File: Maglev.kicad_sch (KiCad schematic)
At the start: 25 parts, among them J1 629722000214, J2 691103110002, J3 61300621121, J4 61300821121, U1 WE-TVS-82400102, U2 ESP32-C3

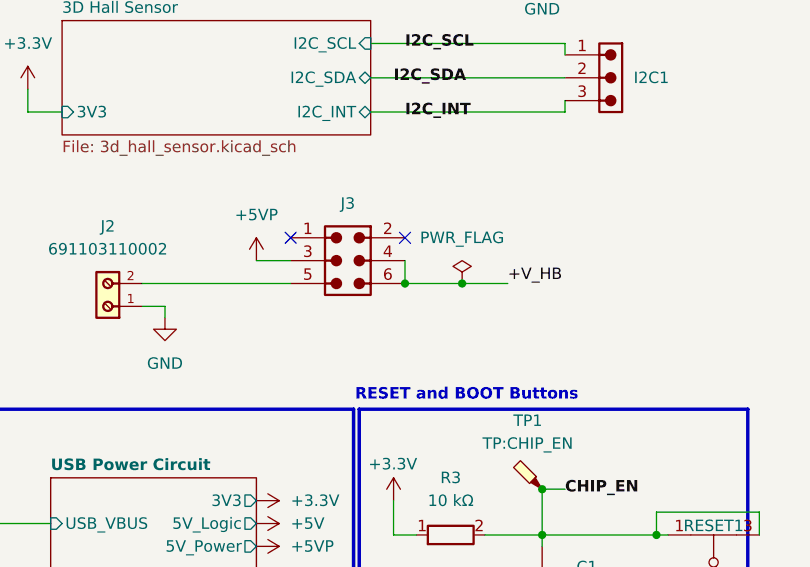
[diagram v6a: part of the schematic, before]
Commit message: Edit symbol libraries for BOM
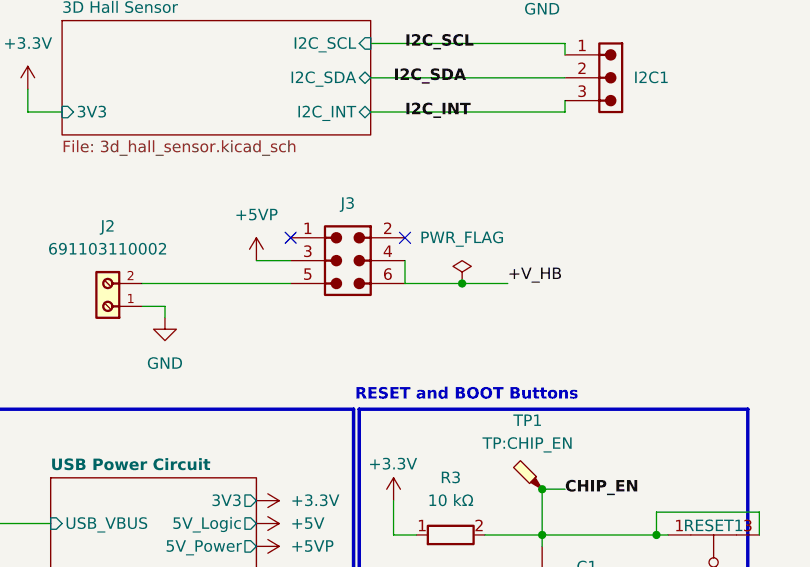
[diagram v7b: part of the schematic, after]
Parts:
- I2C1: symbol Connector_Wurth_WR-PHD:61300311121 -> Connector_Wurth_WR-PHD_CUSTOM:61300311121; Part Number (none) -> 61300311121
- J1: MF Würth Elektronik -> (none); MP 629722000214 -> (none); Manufacturer (none) -> Würth Elektronik; Part Number (none) -> 629722000214
- J2: MF Wurth Electronics -> (none); MP 691103110002 -> (none); Manufacturer (none) -> Wurth Electronics; Part Number (none) -> 691103110002
- J3: symbol Connector_Wurth_WR-PHD:61300621121 -> Connector_Wurth_WR-PHD_CUSTOM:61300621121; Part Number (none) -> 61300621121
- J4: symbol Connector_Wurth_WR-PHD:61300821121 -> Connector_Wurth_WR-PHD_CUSTOM:61300821121; Part Number (none) -> 61300821121
- U1: symbol Power_Protection:WE-TVS-82400102 -> Power_Protection_CUSTOM:WE-TVS-82400102; Manufacturer (none) -> Wurth Elektronik; Part Number (none) -> 82400102
- U2: Manufacturer (none) -> Espressif; Part Number (none) -> ESP32-C3
- UART1: symbol Connector_Wurth_WR-PHD:61300211121 -> Connector_Wurth_WR-PHD_CUSTOM:61300211121; Part Number (none) -> 61300211121
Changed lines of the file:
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@@
 		(color 0 0 0 0)
 	)
-	(junction
-		(at 109.22 116.84)
-		(diameter 0)
-		(color 0 0 0 0)
-	)
 	(no_connect
 		(at 45.72 146.05)
@@
 	)
 	(symbol
-		(lib_id "Connector_Wurth_WR-PHD:61300821121")
+		(lib_id "Connector_Wurth_WR-PHD_CUSTOM:61300821121")
 		(at 140.97 25.4 90)
 		(unit 1)
@@
 			)
 		)
+		(property "Part Number" "61300821121"
+			(at 140.97 25.4 0)
+			(hide yes)
+			(show_name no)
+			(do_not_autoplace no)
+			(effects
+				(font
+					(size 1.27 1.27)
+				)
+			)
+		)
 		(pin "1"
 		)
@@
 			)
 		)
-		(property "Datasheet" ""
+		(property "Datasheet" "https://www.we-online.com/components/products/datasheet/629722000214.pdf?srsltid=AfmBOopgS1fpVqzIp88kkSziMYYixj-iXYRL22aRdxcRBDhgIMAZGuSl"
 			(at 30.48 148.59 0)
 			(hide yes)
@@
 			)
 		)
-		(property "MF" "Würth Elektronik"
+		(property "Package" "None"
 			(at 30.48 148.59 0)
 			(hide yes)
@@
 			)
 		)
-		(property "Package" "None"
+		(property "Price" "None"
 			(at 30.48 148.59 0)
 			(hide yes)
@@
 			)
 		)
-		(property "Price" "None"
+		(property "SnapEDA_Link" "https://www.snapeda.com/parts/629722000214/W%25C3%25BCrth+Elektronik+Midcom/view-part/?ref=snap"
 			(at 30.48 148.59 0)
 			(hide yes)
@@
 			)
 		)
-		(property "SnapEDA_Link" "https://www.snapeda.com/parts/629722000214/W%25C3%25BCrth+Elektronik+Midcom/view-part/?ref=snap"
+		(property "Availability" "In Stock"
 			(at 30.48 148.59 0)
 			(hide yes)
@@
 			)
 		)
-		(property "MP" "629722000214"
+		(property "Check_prices" "https://www.snapeda.com/parts/629722000214/W%25C3%25BCrth+Elektronik+Midcom/view-part/?ref=eda"
 			(at 30.48 148.59 0)
 			(hide yes)
@@
 			)
 		)
-		(property "Availability" "In Stock"
+		(property "Manufacturer" "Würth Elektronik"
 			(at 30.48 148.59 0)
 			(hide yes)
@@
 			)
 		)
-		(property "Check_prices" "https://www.snapeda.com/parts/629722000214/W%25C3%25BCrth+Elektronik+Midcom/view-part/?ref=eda"
+		(property "Part Number" "629722000214"
 			(at 30.48 148.59 0)
 			(hide yes)
@@
 			)
 		)
+		(property "Manufacturer" "Espressif"
+			(at 92.71 52.07 0)
+			(hide yes)
+			(show_name no)
+			(do_not_autoplace no)
+			(effects
+				(font
+					(size 1.27 1.27)
+				)
+			)
+		)
+		(property "Part Number" "ESP32-C3"
+			(at 92.71 52.07 0)
+			(hide yes)
+			(show_name no)
+			(do_not_autoplace no)
+			(effects
+				(font
+					(size 1.27 1.27)
+				)
+			)
+		)
 		(pin "1"
 		)
@@
 	)
 	(symbol
+		(lib_name "ElectromagneticActor_3")
 		(lib_id "Device:ElectromagneticActor")
 		(at 260.35 53.34 180)
@@
 	)
 	(symbol
-		(lib_name "TestPoint_Probe_1")
 		(lib_id "Connector:TestPoint_Probe")
 		(at 124.46 172.72 90)
@@
 	)
 	(symbol
+		(lib_name "ElectromagneticActor_2")
 		(lib_id "Device:ElectromagneticActor")
 		(at 260.35 40.64 180)
@@
 	)
 	(symbol
-		(lib_id "Power_Protection:WE-TVS-82400102")
+		(lib_id "Power_Protection_CUSTOM:WE-TVS-82400102")
 		(at 63.5 162.56 270)
 		(unit 1)
@@
 			)
 		)
+		(property "Manufacturer" "Wurth Elektronik"
+			(at 63.5 162.56 0)
+			(hide yes)
+			(show_name no)
+			(do_not_autoplace no)
+			(effects
+				(font
+					(size 1.27 1.27)
+				)
+			)
+		)
+		(property "Part Number" "82400102"
+			(at 63.5 162.56 0)
+			(hide yes)
+			(show_name no)
+			(do_not_autoplace no)
+			(effects
+				(font
+					(size 1.27 1.27)
+				)
+			)
+		)
 		(pin "6"
 		)
@@
 	)
 	(symbol
+		(lib_name "ElectromagneticActor_1")
 		(lib_id "Device:ElectromagneticActor")
 		(at 260.35 26.67 180)
@@
 	)
 	(symbol
-		(lib_id "Connector_Wurth_WR-PHD:61300621121")
+		(lib_id "Connector_Wurth_WR-PHD_CUSTOM:61300621121")
 		(at 102.87 114.3 270)
 		(unit 1)
@@
 			)
 		)
+		(property "Part Number" "61300621121"
+			(at 102.87 114.3 0)
+			(hide yes)
+			(show_name no)
+			(do_not_autoplace no)
+			(effects
+				(font
+					(size 1.27 1.27)
+				)
+			)
+		)
 		(pin "3"
 		)
@@
 	)
 	(symbol
-		(lib_id "Connector_Wurth_WR-PHD:61300211121")
+		(lib_id "Connector_Wurth_WR-PHD_CUSTOM:61300211121")
 		(at 172.72 24.13 270)
 		(unit 1)
@@
 			)
 		)
+		(property "Part Number" "61300211121"
+			(at 172.72 24.13 0)
+			(hide yes)
+			(show_name no)
+			(do_not_autoplace no)
+			(effects
+				(font
+					(size 1.27 1.27)
+				)
+			)
+		)
 		(pin "1"
 		)
@@
 	)
 	(symbol
-		(lib_id "Connector_Wurth_WR-PHD:61300311121")
+		(lib_id "Connector_Wurth_WR-PHD_CUSTOM:61300311121")
 		(at 132.08 93.98 270)
 		(unit 1)
@@
 			)
 		)
+		(property "Part Number" "61300311121"
+			(at 132.08 93.98 0)
+			(hide yes)
+			(show_name no)
+			(do_not_autoplace no)
+			(effects
+				(font
+					(size 1.27 1.27)
+				)
+			)
+		)
 		(pin "3"
 		)
@@
 			)
 		)
-		(property "Datasheet" ""
+		(property "Datasheet" "https://www.we-online.com/components/products/datasheet/691103110002.pdf"
 			(at 74.93 116.84 0)
 			(hide yes)
@@
 			)
 		)
-		(property "MF" "Wurth Electronics"
+		(property "Package" "None"
 			(at 74.93 116.84 0)
 			(hide yes)
@@
 			)
 		)
-		(property "Package" "None"
+		(property "Price" "None"
 			(at 74.93 116.84 0)
 			(hide yes)
@@
 			)
 		)
-		(property "Price" "None"
+		(property "SnapEDA_Link" "https://www.snapeda.com/parts/691103110002/Wurth+Electronics/view-part/?ref=snap"
 			(at 74.93 116.84 0)
 			(hide yes)
@@
 			)
 		)
-		(property "SnapEDA_Link" "https://www.snapeda.com/parts/691103110002/Wurth+Electronics/view-part/?ref=snap"
+		(property "Purchase-URL" "https://www.snapeda.com/api/url_track_click_mouser/?unipart_id=544489&manufacturer=Wurth Electronics&part_name=691103110002&search_term=None"
 			(at 74.93 116.84 0)
 			(hide yes)
@@
 			)
 		)
-		(property "MP" "691103110002"
+		(property "Availability" "In Stock"
 			(at 74.93 116.84 0)
 			(hide yes)
@@
 			)
 		)
-		(property "Purchase-URL" "https://www.snapeda.com/api/url_track_click_mouser/?unipart_id=544489&manufacturer=Wurth Electronics&part_name=691103110002&search_term=None"
+		(property "Check_prices" "https://www.snapeda.com/parts/691103110002/Wurth+Electronics/view-part/?ref=eda"
 			(at 74.93 116.84 0)
 			(hide yes)
@@
 			)
 		)
-		(property "Availability" "In Stock"
+		(property "Manufacturer" "Wurth Electronics"
 			(at 74.93 116.84 0)
 			(hide yes)
@@
 			)
 		)
-		(property "Check_prices" "https://www.snapeda.com/parts/691103110002/Wurth+Electronics/view-part/?ref=eda"
+		(property "Part Number" "691103110002"
 			(at 74.93 116.84 0)
 			(hide yes)

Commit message: Restliche CUSTOM Librarys comitted und BOM angepasst
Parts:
- U2: symbol MCU_Espressif:ESP32-C3 -> MCU_Espressif_CUSTOM:ESP32-C3
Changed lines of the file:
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@@
 	)
 	(symbol
-		(lib_id "MCU_Espressif:ESP32-C3")
+		(lib_id "MCU_Espressif_CUSTOM:ESP32-C3")
 		(at 92.71 52.07 0)
 		(unit 1)
